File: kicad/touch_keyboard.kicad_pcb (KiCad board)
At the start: 2 copper layers, 68 x 81 mm, 71 parts, among them J1 Conn_02x20_Odd_Even, J2 OUT, J3 Barrel_Jack_Switch, J4 Conn_01x04_Pin, Q1 BC846, Q2 BC846, SW1 SW_Push, U1 Pico

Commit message: circuit update
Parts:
- added H3: MountingHole_Pad, MountingHole:MountingHole_3.2mm_M3_DIN965_Pad, F.Cu at (187.2, 57.5)
- added H4: MountingHole_Pad, MountingHole:MountingHole_3.2mm_M3_DIN965_Pad, F.Cu at (97.2, 57.5)
- added J5: power, Connector_PinHeader_2.54mm:PinHeader_1x02_P2.54mm_Horizontal, F.Cu at (187.2, 89.5)
- added R39: 100k, Resistor_SMD:R_0603_1608Metric, F.Cu at (159.2, 79.5)
- added SW2: BT2, 0_local:Button, F.Cu at (107.2, 99.5)
- C18, C19: value 1uF -> 10uF
- D1: value MBR0530 -> SK24A; footprint Diode_SMD:D_SOD-123 -> Diode_SMD:D_SMA-SMB_Universal_Handsoldering
- D2, D3: value MBR0530 -> BAT43; footprint Diode_SMD:D_SOD-123 -> Diode_SMD:D_MiniMELF
- J4: footprint Connector_PinHeader_2.54mm:PinHeader_1x04_P2.54mm_Horizontal -> Connector_PinHeader_2.54mm:PinHeader_1x03_P2.54mm_Horizontal
- R37: value 10k -> 1k
- RV1: footprint Potentiometer_THT:Potentiometer_Bourns_PTV09A-1_Single_Vertical -> 0_local:Potentiometer_Bourns_PTV09A-1_Single_Vertical
- SW1: value SW_Push -> Calibrate; footprint Button_Switch_THT:SW_PUSH-12mm -> 0_local:Button
- moved R38 48.1 mm to (157.2, 77.5), turned to 180 degrees
- moved RV1 16.5 mm to (177.2, 84.5)
- moved D2 14.5 mm to (125.3, 62.2)
- moved Q1 14.0 mm to (124.5, 58.1)
- moved R35 13.6 mm to (126.6, 54.6), turned to 180 degrees
- moved R37 12.6 mm to (163.8, 107.1)
- moved SW1 9.90 mm to (107.2, 84.5), turned to 180 degrees
- moved R34 7.67 mm to (123.2, 65.6), turned to -90 degrees
- moved J3 5.66 mm to (175.3, 64.2)
- moved J4 5.39 mm to (167.6, 102.9), turned to 0 degrees
- moved C17 5.08 mm to (110.2, 72.4)
- moved J2 5.08 mm to (111.8, 59.7)
- moved R33 5.08 mm to (110.0, 69.8)
- moved C18 5.02 mm to (164.1, 65.5), turned to 90 degrees
- moved D1 2.89 mm to (162.6, 58.5), turned to -90 degrees
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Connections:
- J4 pad 2: +5V -> Net-(D3-K)
- J4 pad 3: Net-(D3-K) -> +5V
- RV1 pad 1: GND -> /VREF
- RV1 pad 3: Net-(U1-ADC_VREF) -> GND
- SW1 pad 2: /bt_in -> /cal_bt
- U1 pad 1: unconnected-(U1-GPIO0-Pad1) -> /TX
- U1 pad 29: /mode -> unconnected-(U1-GPIO22-Pad29)
- U1 pad 31: /led_out -> /mode
- U1 pad 32: unconnected-(U1-GPIO27_ADC1-Pad32) -> /led_out
- U1 pad 35: Net-(U1-ADC_VREF) -> /VREF
- U1 pad 6: /TX -> /cal_bt
- U1 pad 7: /bt_in -> /bt2
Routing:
- net /bt2: track 0.00 -> 69.5 mm, vias 0 -> 1
- net /cal_bt: track 0.00 -> 58.7 mm, vias 0 -> 1
- net Net-(J1-Pin_1): track 2.80 -> 54.3 mm
- net /VREF: track 0.00 -> 48.7 mm, vias 0 -> 2
- net Net-(D1-A): track 15.2 -> 59.7 mm
- net /mode: track 49.1 -> 5.21 mm
- net +5V: track 113.1 -> 148.7 mm
- net /bt_in: track 33.4 -> 0.00 mm, vias 1 -> 0
- net Net-(U1-ADC_VREF): track 26.7 -> 0.00 mm, vias 1 -> 0
- net GND: track 71.2 -> 85.0 mm, vias 28 -> 29
- net /led_out: track 25.3 -> 29.9 mm
- net Net-(J2-Pad5): track 7.99 -> 11.6 mm
- net Net-(D3-K): track 11.6 -> 15.1 mm
- net Net-(U1-GPIO28_ADC2): track 25.6 -> 28.7 mm, vias 1 -> 0
- net Net-(D2-A): track 10.8 -> 8.60 mm
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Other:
- board size 68 x 81 mm -> 100 x 81 mm

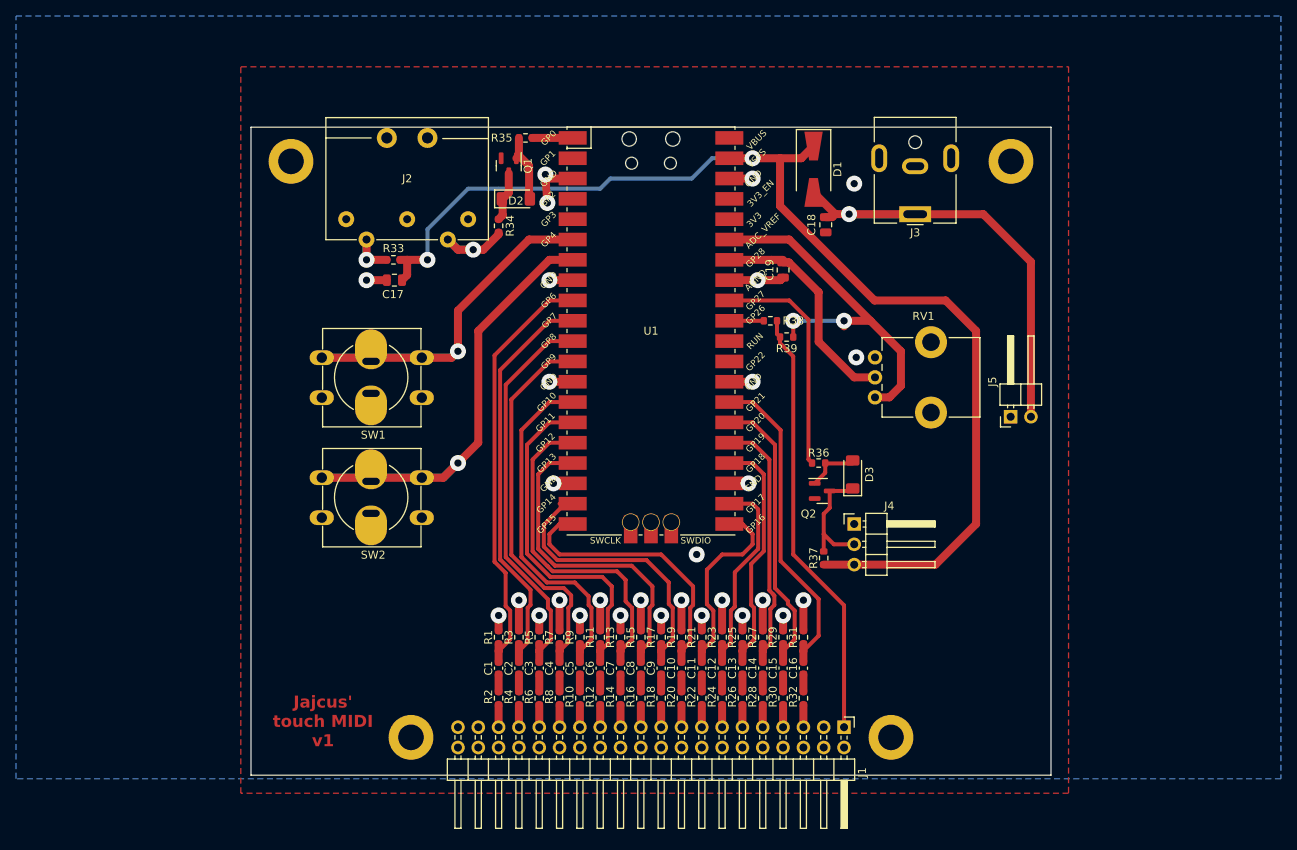
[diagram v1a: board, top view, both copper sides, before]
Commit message: update to the current version of the hardware
includes pcb2gcode config and post-processing script
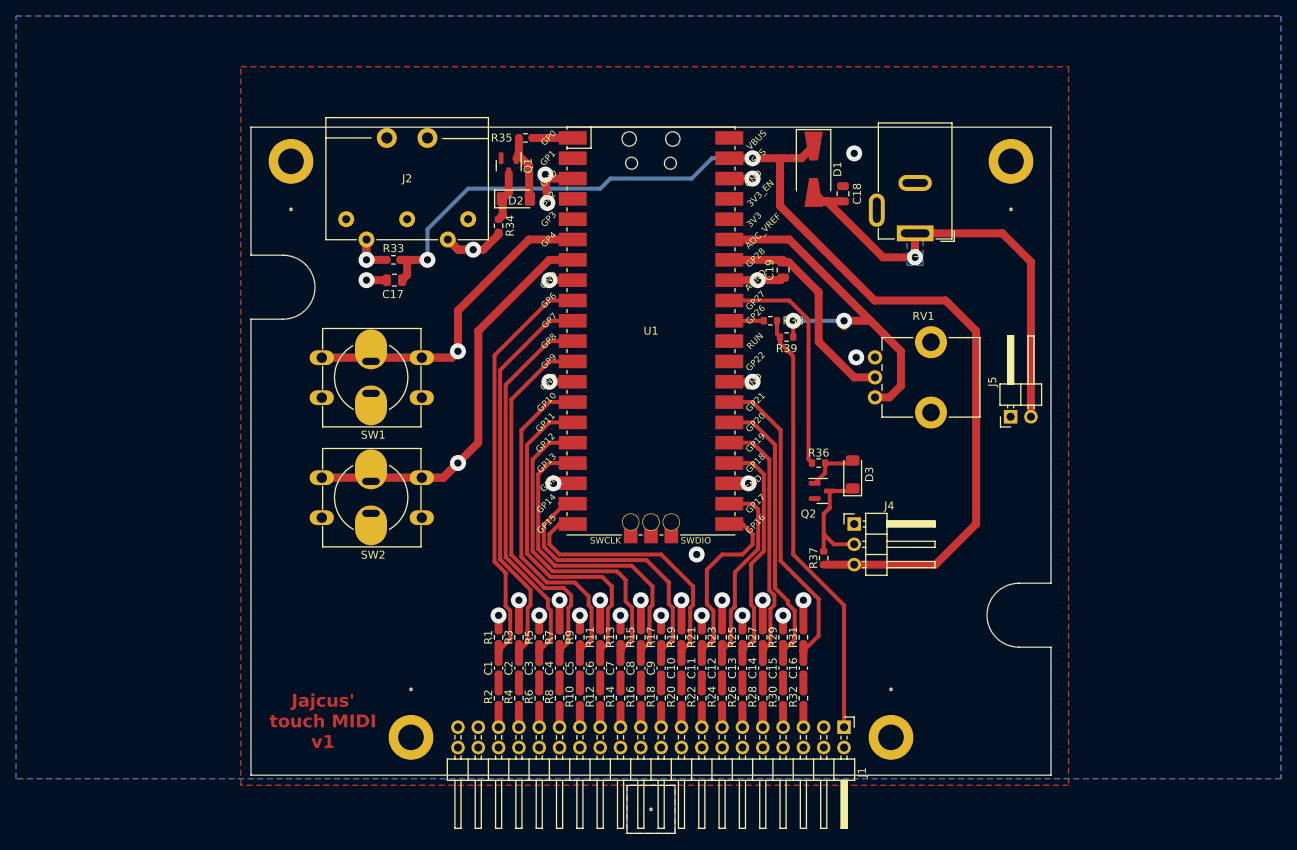
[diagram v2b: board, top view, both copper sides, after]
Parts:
- added REF**: align_marker, 0_local:align_marker, F.Cu at (112.2, 123.5)
- added REF**: align_marker, 0_local:align_marker, F.Cu at (187.2, 63.5)
- added REF**: align_marker, 0_local:align_marker, F.Cu at (172.2, 123.5)
- added REF**: align_marker, 0_local:align_marker, F.Cu at (142.2, 138.5)
- added REF**: align_marker, 0_local:align_marker, F.Cu at (97.2, 63.5)
- J3: footprint Connector_BarrelJack:BarrelJack_CUI_PJ-063AH_Horizontal -> Connector_BarrelJack:BarrelJack_GCT_DCJ200-10-A_Horizontal
- moved C18 4.44 mm to (166.2, 61.6), turned to -90 degrees
- moved J3 2.39 mm to (175.3, 66.5)
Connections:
- net Net-(D1-A) renamed /p+
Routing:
- net /p+: track 59.7 -> 56.9 mm
- net GND: track 85.0 -> 86.4 mm
- added copper zone on B.Cu, net /p+
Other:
- board size 100 x 81 mm -> 100 x 88.3 mm
